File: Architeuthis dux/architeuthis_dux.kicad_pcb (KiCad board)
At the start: 2 copper layers, 129.3 x 96.3 mm, 36 parts

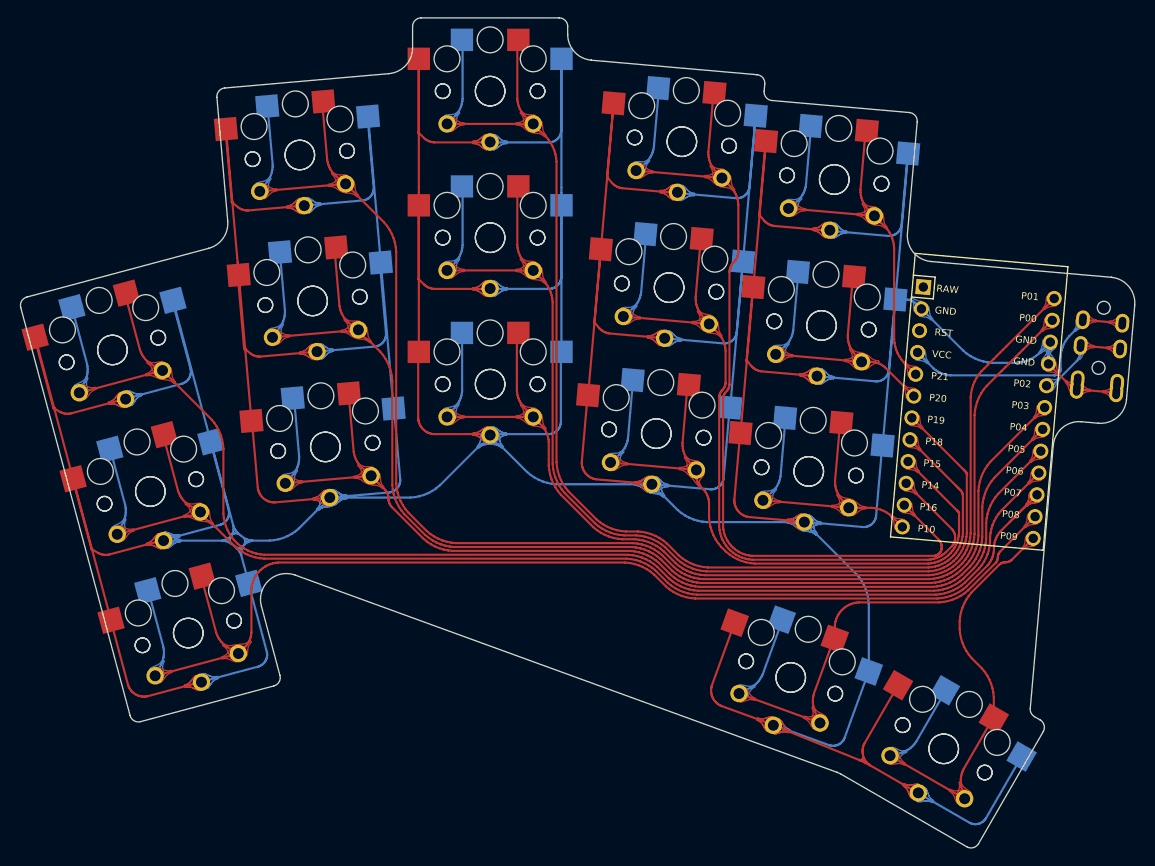
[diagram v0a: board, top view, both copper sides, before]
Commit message: Added tenting puck support to A. dux
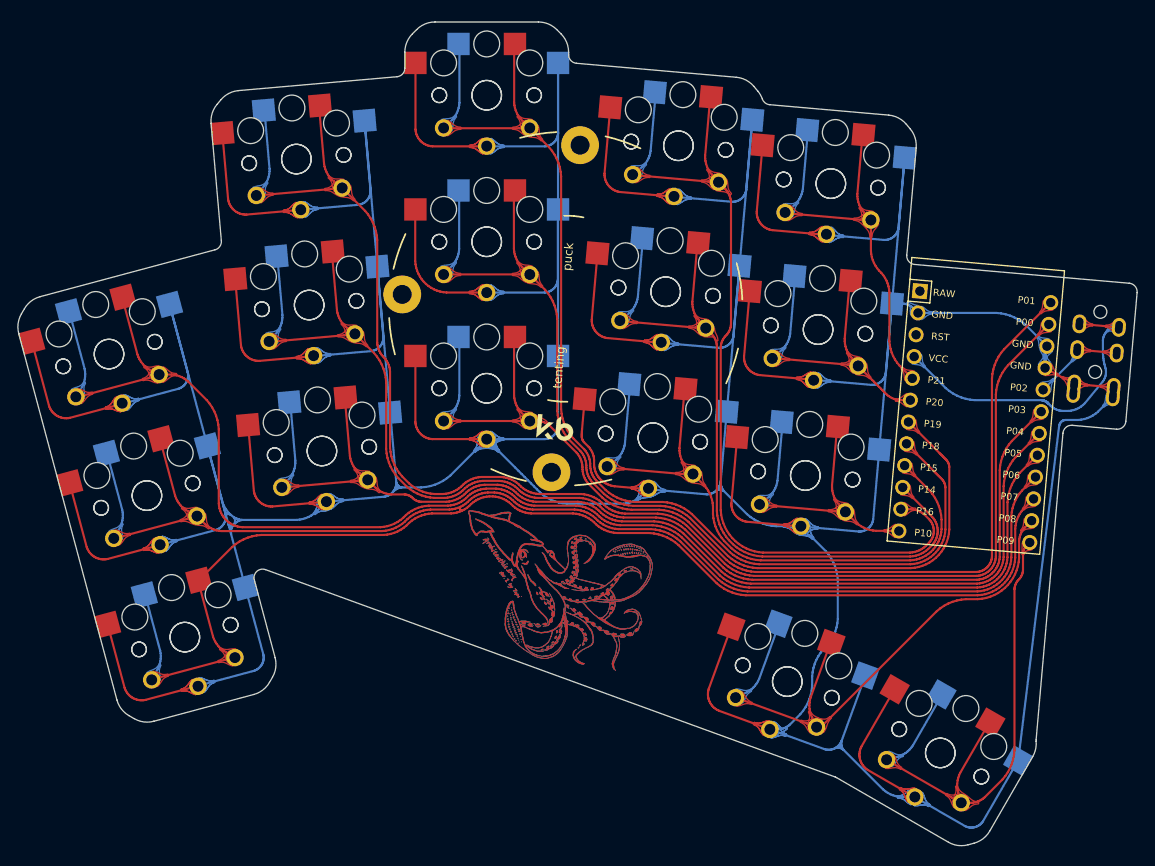
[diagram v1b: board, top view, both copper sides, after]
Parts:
- removed the REF** at (122.3, -38.6)
- added G***: LOGO, Kicad:squid_1500, F.Cu at (56.0, -4.65)
- added REF**: Tenting Puck, Kicad:Tenting_Puck, F.Cu at (57.4, -37.0)
- added T1: , TRRS-PJ-320A-dual, F.Cu at (121.9, -38.1)
- moved S3 0.62 mm to (8.80, -15.4)
- moved S4 0.62 mm to (8.80, -15.4)
- moved S5 0.62 mm to (4.40, -31.8)
- moved S6 0.62 mm to (4.40, -31.8)
- moved S10 0.62 mm to (27.6, -37.5)
- moved S9 0.62 mm to (27.6, -37.5)
- moved S31 0.62 mm to (83.1, 6.21)
- moved S32 0.62 mm to (83.1, 6.21)
- moved S19 0.62 mm to (67.5, -22.1)
- moved S20 0.62 mm to (67.5, -22.1)
- moved S1 0.62 mm to (13.2, 1.05)
- moved S2 0.62 mm to (13.2, 1.05)
- moved S17 0.62 mm to (48.2, -61.8)
- moved S18 0.62 mm to (48.2, -61.8)
- moved C1 0.62 mm to (104.9, -24.5)
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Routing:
- net GND: track 1083.8 -> 944.7 mm
- net VCC: track 29.2 -> 40.0 mm
- net P19: track 125.5 -> 117.4 mm
- net P18: track 138.5 -> 130.5 mm
- net P9: track 56.4 -> 63.4 mm
- net P14: track 94.2 -> 87.6 mm
- net P15: track 80.8 -> 75.0 mm
- net P8: track 61.1 -> 66.1 mm
- net P16: track 106.6 -> 102.0 mm
- net P6: track 138.3 -> 141.7 mm
- net P5: track 158.0 -> 161.1 mm
- net P1: track 124.9 -> 127.5 mm
- net P7: track 143.0 -> 140.7 mm
- net P0: track 170.6 -> 169.2 mm
- net P21: track 50.4 -> 49.1 mm
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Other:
- board size 129.3 x 96.3 mm -> 129.9 x 95.6 mm

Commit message: Fixed routing artifact
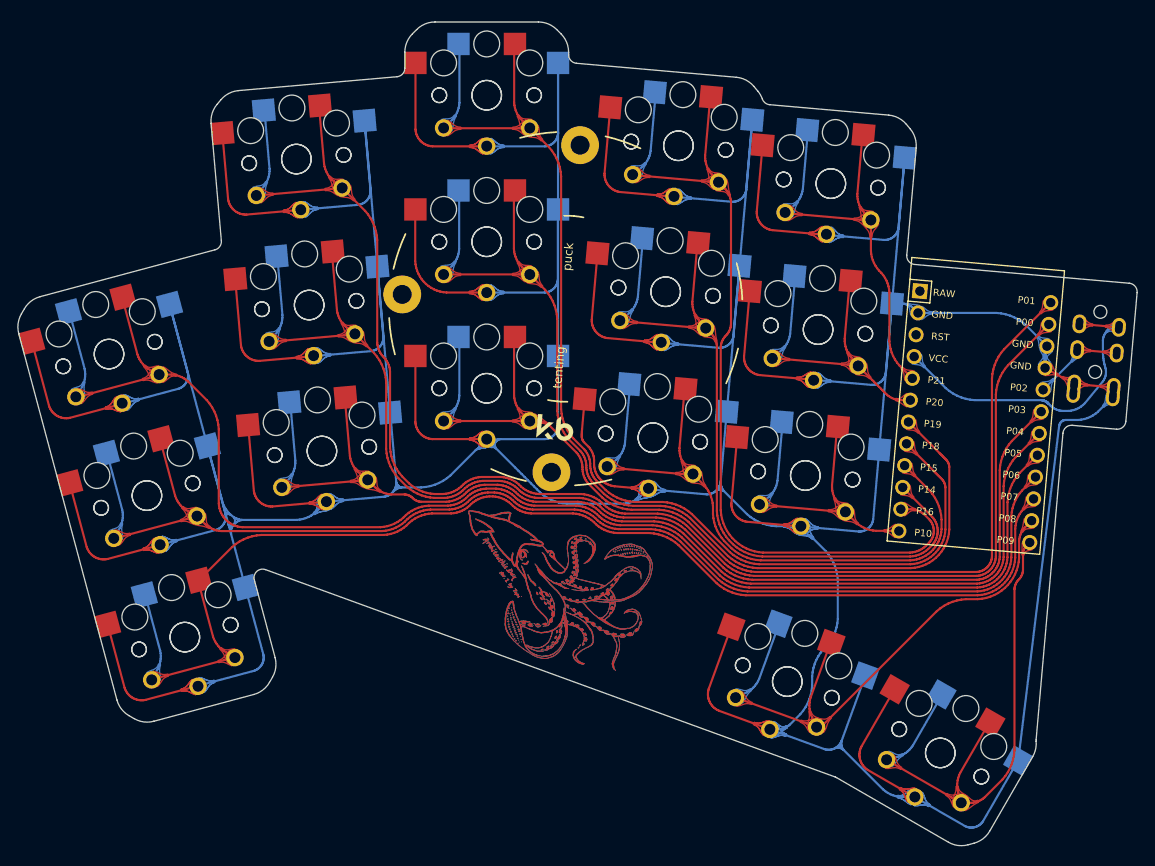
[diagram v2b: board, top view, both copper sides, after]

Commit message: Updated logo and fixed routing
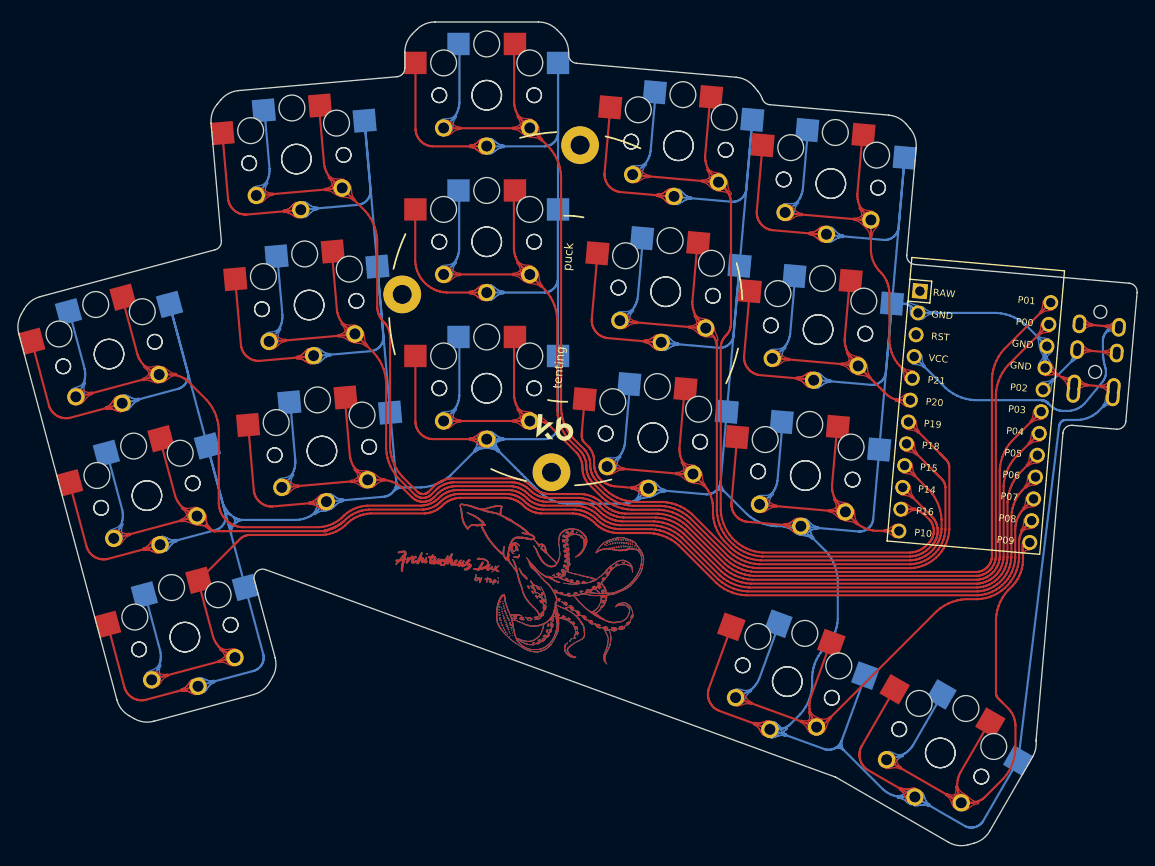
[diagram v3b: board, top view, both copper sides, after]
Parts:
- G***: footprint Kicad:squid_1500 -> Kicad:squid_perce_test_text
- moved G*** 3.32 mm to (52.9, -5.78)
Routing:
- net P6: track 141.7 -> 160.1 mm
- net P9: track 63.4 -> 66.4 mm

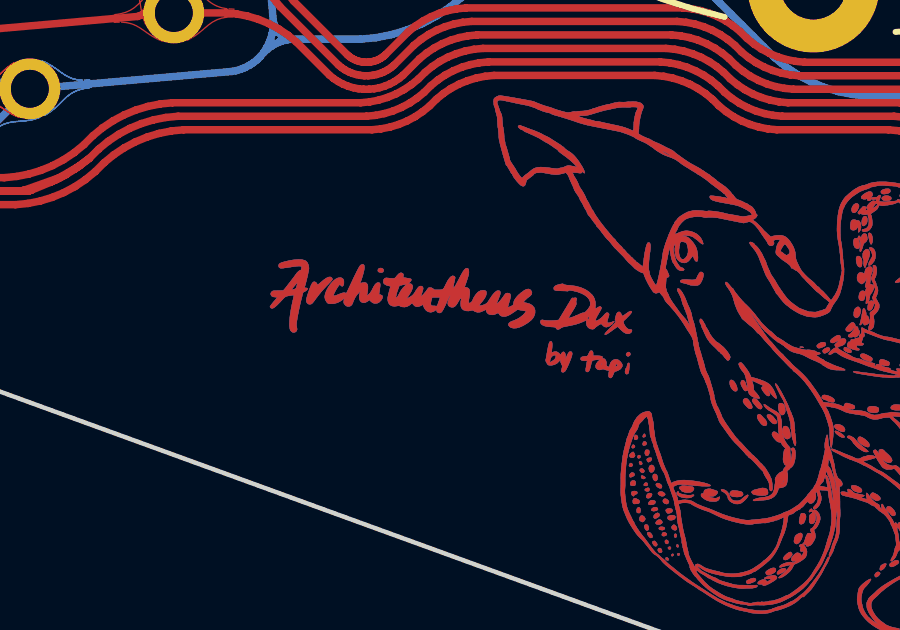
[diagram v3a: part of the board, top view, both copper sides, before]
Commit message: Fixed text on back side
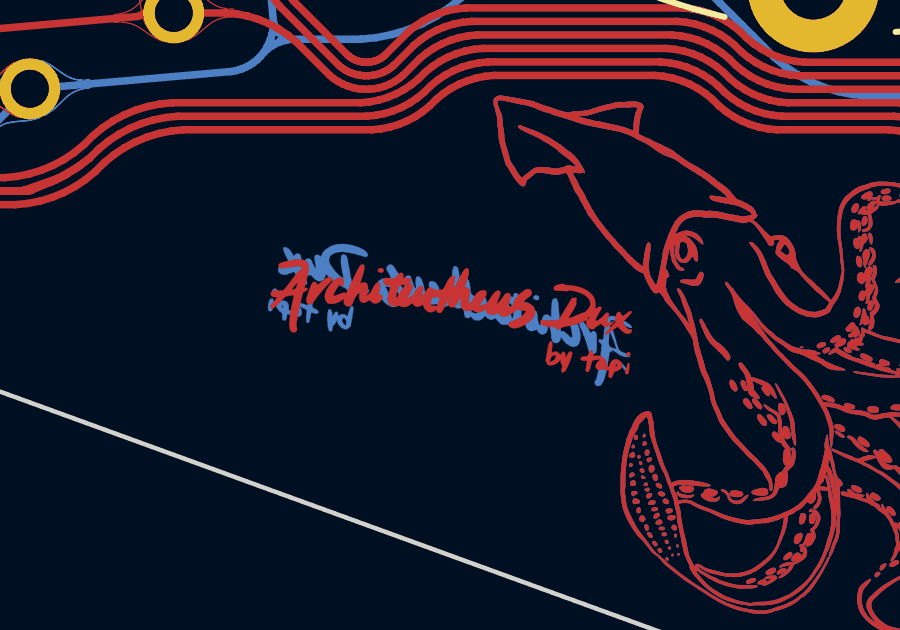
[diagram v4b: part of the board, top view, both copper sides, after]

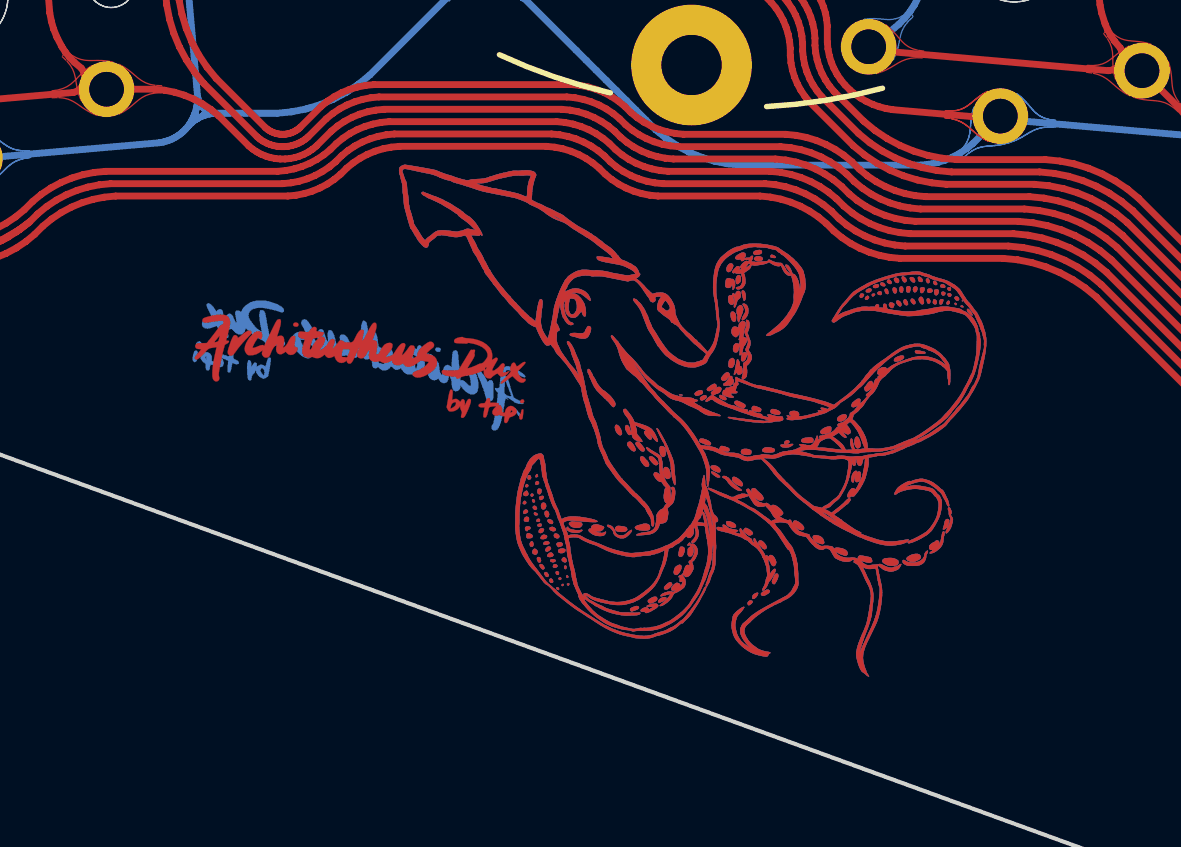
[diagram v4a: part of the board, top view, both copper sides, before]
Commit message: Increased font size
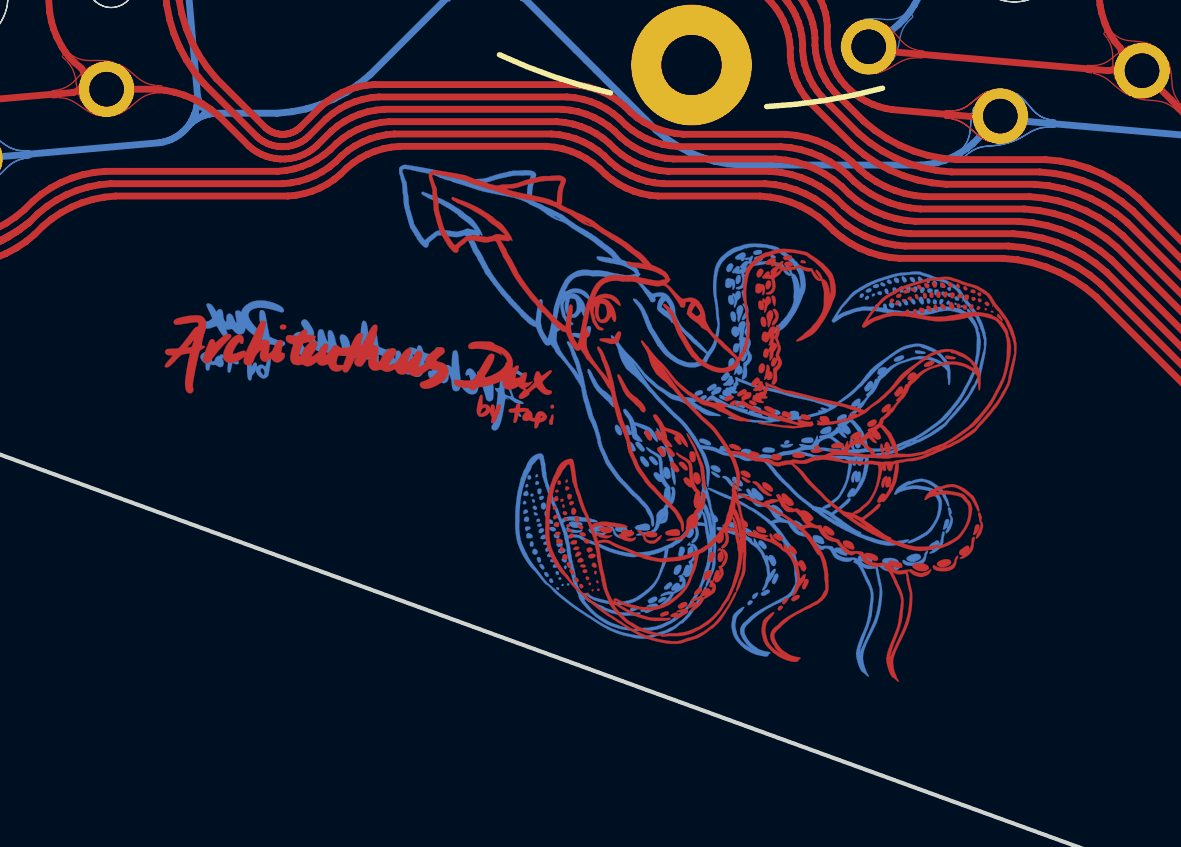
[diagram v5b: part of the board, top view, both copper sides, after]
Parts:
- G***: footprint Kicad:squid_perce_test_text -> Kicad:BIGSQUID

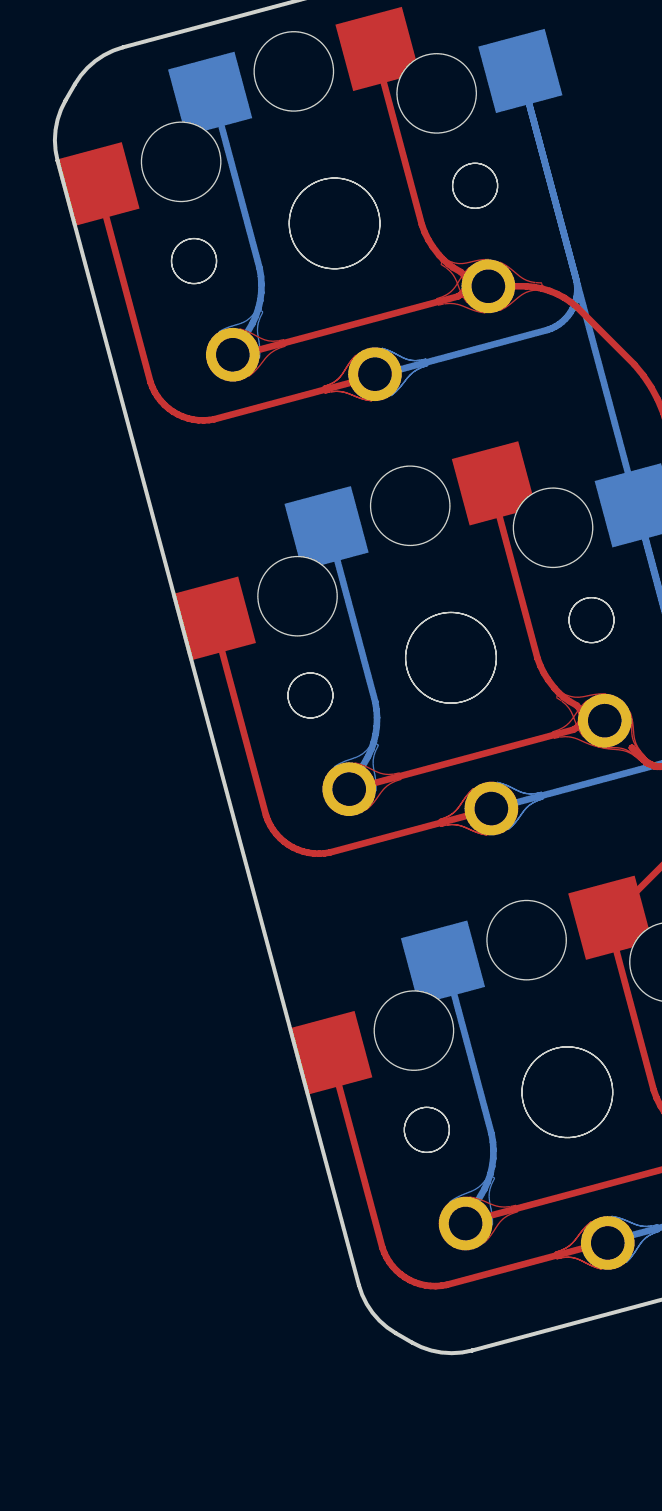
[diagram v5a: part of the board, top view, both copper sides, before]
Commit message: Remove phantom drill holes on pinkie edge
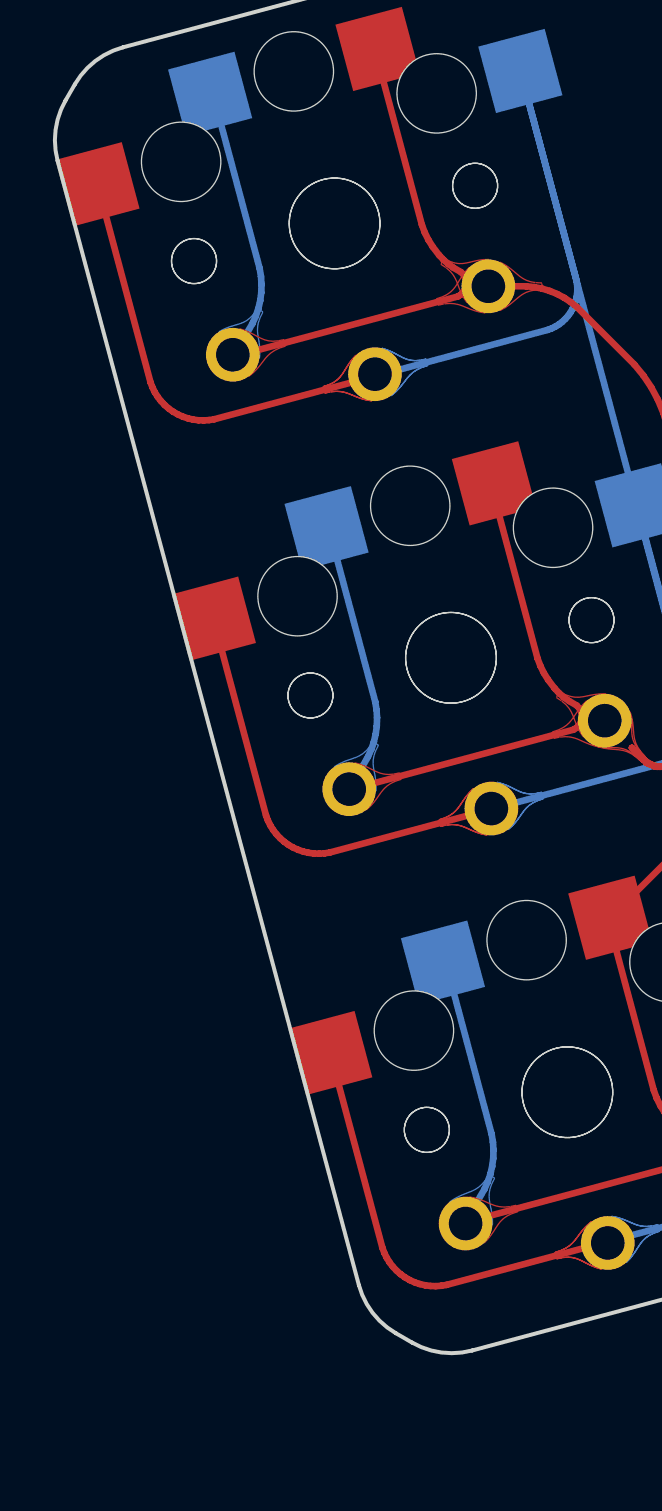
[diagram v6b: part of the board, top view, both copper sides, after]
